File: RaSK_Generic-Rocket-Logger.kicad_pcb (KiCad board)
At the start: 2 copper layers, 30 x 70 mm, 51 parts, among them J1 SD_Card, J2 TWE_Writer, J3 GS2, J4 Mount, J5 Mount, J6 Mount, J7 Mount, P1 STLINK_SWD, P2 KRC_PSoCWriter, P3 TRIGOUT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

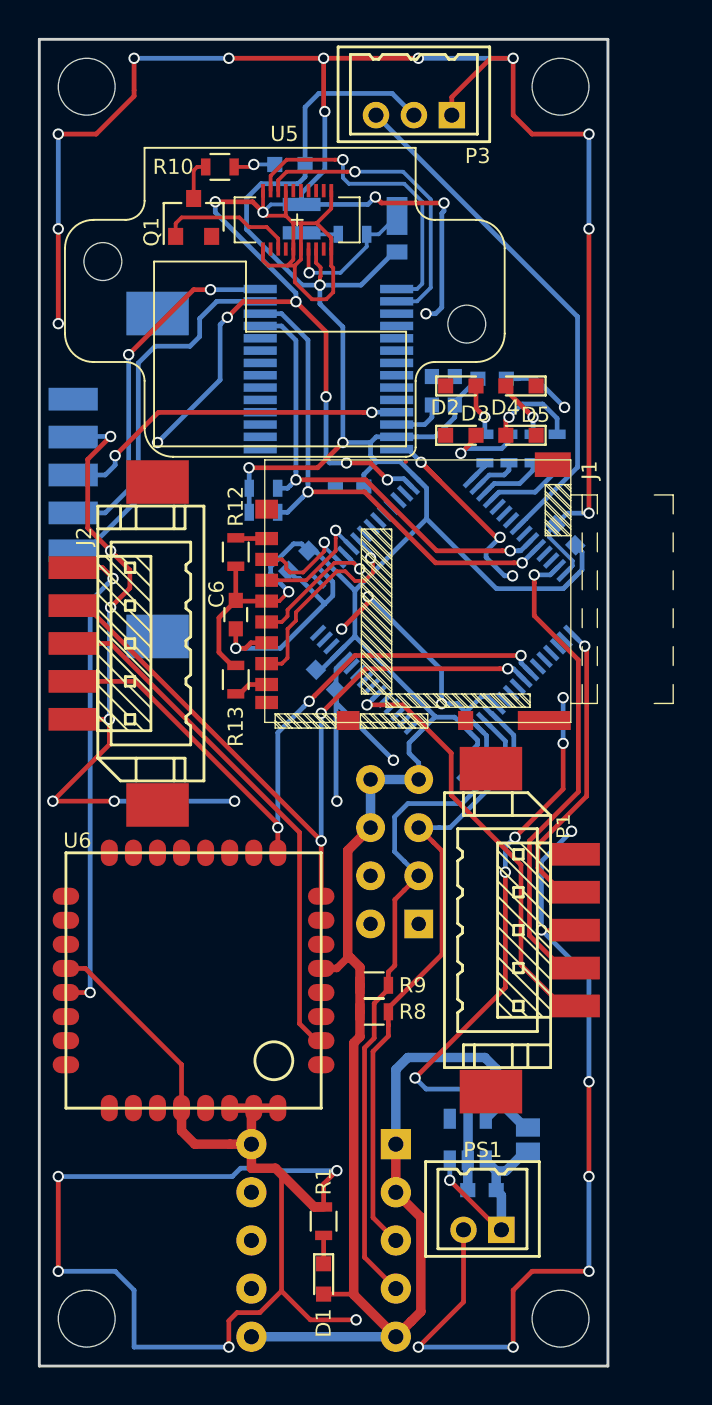
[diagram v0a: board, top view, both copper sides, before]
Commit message: add buzzer out and trigger pin to port
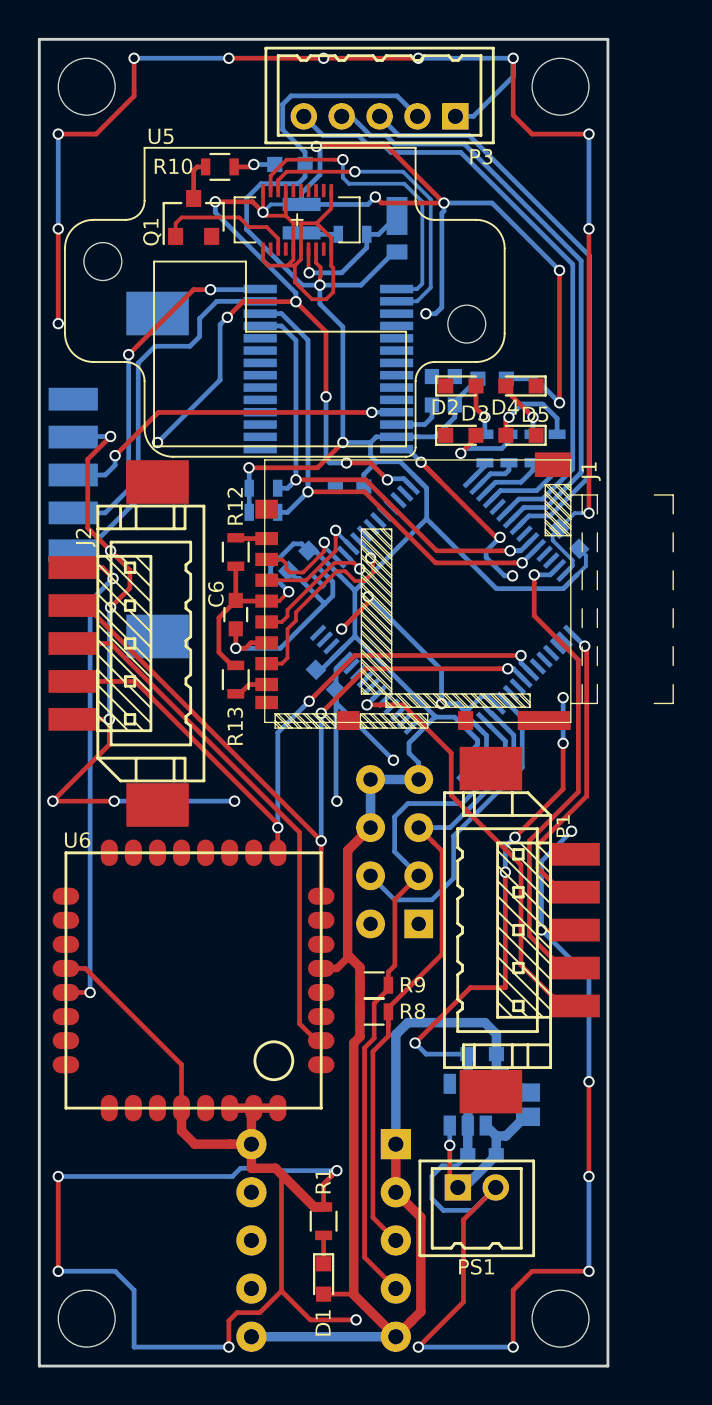
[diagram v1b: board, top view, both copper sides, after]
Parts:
- P3: value TRIGOUT -> PORT; footprint KUT_Connector:DF3A-3P-2DSA -> KUT_Connector:DF3A-5P-2DSA
- moved PS1 2.26 mm to (123.1, 160.6), turned to 180 degrees
- moved C1 1.84 mm to (123.4, 158.9)
- moved C2 1.84 mm to (123.4, 153.5)
- moved J3 1.84 mm to (125.8, 156.2)
- moved VR1 1.84 mm to (122.6, 156.2)
- moved P3 1.81 mm to (118.0, 104.1)
- moved C9 0.28 mm to (128.0, 126.4)
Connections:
- net /TRIGSIG renamed /TRIG
- U1 pad 38: (no net) -> /BUZZ
- U1 pad 39: (no net) -> /FPIN
- U1 pad 59: (no net) -> /LPS22HB_DRDY
- U3 pad 6: (no net) -> /LPS22HB_DRDY
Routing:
- net /BUZZ: track 0.00 -> 32.8 mm
- net /FPIN: track 0.00 -> 31.7 mm
- net GND: track 406.5 -> 433.2 mm, vias 57 -> 58
- net /LPS22HB_DRDY: track 0.00 -> 16.7 mm
- net +3V3: track 187.1 -> 190.8 mm
- net /TRIG: track 27.4 -> 30.7 mm
- net +6V: track 11.0 -> 10.1 mm

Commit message: board released
とりあえず完成品
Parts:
- added G***: LOGO, user_temp:rask, B.Cu at (105.1, 158.9)
- added G***: YUYUSHIKI_LOGO, user_temp:yuyushiki_logo, B.Cu at (124.9, 109.9)
- added G***: LOGO, user_temp:generalrocketlogger, F.Cu at (104.1, 159.8)
- added P4: UARTDebug, Pin_Headers:Pin_Header_Straight_1x04_Pitch2.54mm, B.Cu at (128.3, 162.4)
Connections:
- P3 pad 4: /FPIN -> /BUZZ
- P3 pad 5: /BUZZ -> /FPIN
- U1 pad 22: /SD_MOSI -> /SD_MISO
- U1 pad 23: /SD_MISO -> /SD_MOSI
- U1 pad 38: /BUZZ -> /FPIN
- U1 pad 39: /FPIN -> /BUZZ
- U1 pad 51: (no net) -> /Debug_MOUT
- U1 pad 52: (no net) -> /Debug_MIN
- U1 pad 55: /TWE_MIN -> /TWE_MOUT
- U1 pad 56: /TWE_MOUT -> /TWE_MIN
- U6 pad 8: /TWE_MOUT -> /TWE_MIN
- U6 pad 9: /TWE_MIN -> /TWE_MOUT
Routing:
- net /Debug_MIN: track 0.00 -> 27.0 mm
- net /Debug_MOUT: track 0.00 -> 24.0 mm
- net GND: track 433.2 -> 428.9 mm, vias 58 -> 59
- net /TWE_MIN: track 36.1 -> 39.0 mm, vias 3 -> 4
- net /TWE_MOUT: track 39.8 -> 37.6 mm, vias 3 -> 4
- net /SD_MISO: track 11.2 -> 9.65 mm
- net /FPIN: track 31.7 -> 32.8 mm
- net /BUZZ: track 32.8 -> 31.7 mm
- net /SD_CLK: track 7.66 -> 6.82 mm
